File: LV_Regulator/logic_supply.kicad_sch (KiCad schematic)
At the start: 19 parts, among them IC2 MIC29152WU, IC3 MIC29152WU

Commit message: Added Footprints & Links for Component Purchase
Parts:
- C10, C7: footprint (none) -> Capacitor_SMD:C_1206_3216Metric_Pad1.33x1.80mm_HandSolder; Purchase Place (none) -> https://eu.mouser.com/ProductDetail/KYOCERA-AVX/12066G106ZA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
- C11, C8: footprint (none) -> Capacitor_SMD:C_1206_3216Metric_Pad1.33x1.80mm_HandSolder; Purchase Place (none) -> https://eu.mouser.com/ProductDetail/Murata-Electronics/GGM3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
- C9: footprint (none) -> Capacitor_SMD:C_1206_3216Metric_Pad1.33x1.80mm_HandSolder; Purchase Place (none) -> https://eu.mouser.com/ProductDetail/TAIYO-YUDEN/MLASJ319LB5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
- D2, D3, D4, D5: footprint (none) -> SS14:CR_SMA_403AE_OSI; Purchase Place (none) -> https://www.digikey.com/en/products/detail/onsemi/ss14/9654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
- F2, F3: footprint (none) -> Fuse:Fuse_1206_3216Metric_Pad1.42x1.75mm_HandSolder; Purchase Place (none) -> https://eu.mouser.com/ProductDetail/Bourns/SF-1206S100-2?qs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
- IC2, IC3: footprint MIC29152WU -> MIC29152WU:MIC29152WU
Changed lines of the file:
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@@
 			)
 		)
-		(property "Footprint" "MIC29152WU"
+		(property "Footprint" "MIC29152WU:MIC29152WU"
 			(at 109.22 134.29 0)
 			(effects
@@
 			)
 		)
-		(property "Footprint" ""
+		(property "Footprint" "SS14:CR_SMA_403AE_OSI"
 			(at 50.8 101.6 0)
 			(effects
@@
 		)
 		(property "Sim.Pins" "1=K 2=A"
+			(at 50.8 101.6 0)
+			(effects
+				(font
+					(size 1.27 1.27)
+				)
+				(hide yes)
+			)
+		)
+		(property "Purchase Place" "https://www.digikey.com/en/products/detail/onsemi/ss14/965474"
 			(at 50.8 101.6 0)
 			(effects
@@
 			)
 		)
-		(property "Footprint" ""
+		(property "Footprint" "Capacitor_SMD:C_1206_3216Metric_Pad1.33x1.80mm_HandSolder"
 			(at 82.2452 95.25 0)
 			(effects
@@
 		)
 		(property "Description" "Unpolarized capacitor"
+			(at 81.28 91.44 0)
+			(effects
+				(font
+					(size 1.27 1.27)
+				)
+				(hide yes)
+			)
+		)
+		(property "Purchase Place" "https://eu.mouser.com/ProductDetail/KYOCERA-AVX/12066G106ZAT4A?qs=f21FSZc47Pg9KHN6RDKhaQ%3D%3D"
 			(at 81.28 91.44 0)
 			(effects
@@
 			)
 		)
-		(property "Footprint" ""
+		(property "Footprint" "Fuse:Fuse_1206_3216Metric_Pad1.42x1.75mm_HandSolder"
 			(at 60.96 103.378 90)
 			(effects
@@
 		(property "Description" "Fuse"
 			(at 60.96 101.6 0)
+			(effects
+				(font
+					(size 1.27 1.27)
+				)
+				(hide yes)
+			)
+		)
+		(property "Purchase Place" "https://eu.mouser.com/ProductDetail/Bourns/SF-1206S100-2?qs=GIQXYiEeHGDIjBsMHQBJ8g%3D%3D"
+			(at 60.96 101.6 90)
 			(effects
 				(font
@@
 			)
 		)
-		(property "Footprint" ""
+		(property "Footprint" "Capacitor_SMD:C_1206_3216Metric_Pad1.33x1.80mm_HandSolder"
 			(at 42.8752 46.99 0)
 			(effects
@@
 		)
 		(property "Description" "Unpolarized capacitor"
+			(at 41.91 50.8 0)
+			(effects
+				(font
+					(size 1.27 1.27)
+				)
+				(hide yes)
+			)
+		)
+		(property "Purchase Place" "https://eu.mouser.com/ProductDetail/TAIYO-YUDEN/MLASJ319LB5476MTNA01?qs=tlsG%2FOw5FFj12GZbAd1Q9Q%3D%3D"
 			(at 41.91 50.8 0)
 			(effects
@@
 			)
 		)
-		(property "Footprint" "MIC29152WU"
+		(property "Footprint" "MIC29152WU:MIC29152WU"
 			(at 111.76 188.9 0)
 			(effects
@@
 			)
 		)
-		(property "Footprint" ""
+		(property "Footprint" "SS14:CR_SMA_403AE_OSI"
 			(at 50.8 46.99 0)
 			(effects
@@
 		)
 		(property "Sim.Pins" "1=K 2=A"
+			(at 50.8 46.99 0)
+			(effects
+				(font
+					(size 1.27 1.27)
+				)
+				(hide yes)
+			)
+		)
+		(property "Purchase Place" "https://www.digikey.com/en/products/detail/onsemi/ss14/965474"
 			(at 50.8 46.99 0)
 			(effects
@@
 			)
 		)
-		(property "Footprint" ""
+		(property "Footprint" "Capacitor_SMD:C_1206_3216Metric_Pad1.33x1.80mm_HandSolder"
 			(at 70.8152 101.6 0)
 			(effects
@@
 		)
 		(property "Description" "Unpolarized capacitor"
+			(at 69.85 105.41 0)
+			(effects
+				(font
+					(size 1.27 1.27)
+				)
+				(hide yes)
+			)
+		)
+		(property "Purchase Place" "https://eu.mouser.com/ProductDetail/Murata-Electronics/GGM31CD70J226KE02L?qs=efUn273yAheMi1mARkgjog%3D%3D"
 			(at 69.85 105.41 0)
 			(effects
@@
 			)
 		)
-		(property "Footprint" ""
+		(property "Footprint" "Capacitor_SMD:C_1206_3216Metric_Pad1.33x1.80mm_HandSolder"
 			(at 70.8152 46.99 0)
 			(effects
@@
 			)
 		)
+		(property "Purchase Place" "https://eu.mouser.com/ProductDetail/Murata-Electronics/GGM31CD70J226KE02L?qs=efUn273yAheMi1mARkgjog%3D%3D"
+			(at 69.85 50.8 0)
+			(effects
+				(font
+					(size 1.27 1.27)
+				)
+				(hide yes)
+			)
+		)
 		(pin "1"
 		)
@@
 			)
 		)
-		(property "Footprint" ""
+		(property "Footprint" "Capacitor_SMD:C_1206_3216Metric_Pad1.33x1.80mm_HandSolder"
 			(at 79.7052 40.64 0)
 			(effects
@@
 		)
 		(property "Description" "Unpolarized capacitor"
+			(at 78.74 36.83 0)
+			(effects
+				(font
+					(size 1.27 1.27)
+				)
+				(hide yes)
+			)
+		)
+		(property "Purchase Place" "https://eu.mouser.com/ProductDetail/KYOCERA-AVX/12066G106ZAT4A?qs=f21FSZc47Pg9KHN6RDKhaQ%3D%3D"
 			(at 78.74 36.83 0)
 			(effects
@@
 			)
 		)
-		(property "Footprint" ""
+		(property "Footprint" "SS14:CR_SMA_403AE_OSI"
 			(at 44.45 92.71 0)
 			(effects
@@
 		(property "Sim.Pins" "1=K 2=A"
 			(at 44.45 92.71 0)
+			(effects
+				(font
+					(size 1.27 1.27)
+				)
+				(hide yes)
+			)
+		)
+		(property "Purchase Place" "https://www.digikey.com/en/products/detail/onsemi/ss14/965474"
+			(at 44.45 92.71 90)
 			(effects
 				(font
@@
 			)
 		)
-		(property "Footprint" ""
+		(property "Footprint" "Fuse:Fuse_1206_3216Metric_Pad1.42x1.75mm_HandSolder"
 			(at 62.23 48.768 90)
 			(effects
@@
 		(property "Description" "Fuse"
 			(at 62.23 46.99 0)
+			(effects
+				(font
+					(size 1.27 1.27)
+				)
+				(hide yes)
+			)
+		)
+		(property "Purchase Place" "https://eu.mouser.com/ProductDetail/Bourns/SF-1206S100-2?qs=GIQXYiEeHGDIjBsMHQBJ8g%3D%3D"
+			(at 62.23 46.99 90)
 			(effects
 				(font
@@
 			)
 		)
-		(property "Footprint" ""
+		(property "Footprint" "SS14:CR_SMA_403AE_OSI"
 			(at 44.45 39.37 0)
 			(effects
@@
 			(effects
 				(font
+					(size 1.27 1.27)
+				)
+				(hide yes)
+			)
+		)
+		(property "Purchase Place" "https://www.digikey.com/en/products/detail/onsemi/ss14/965474"
+			(at 44.45 39.37 90)
+			(effects
+				(font

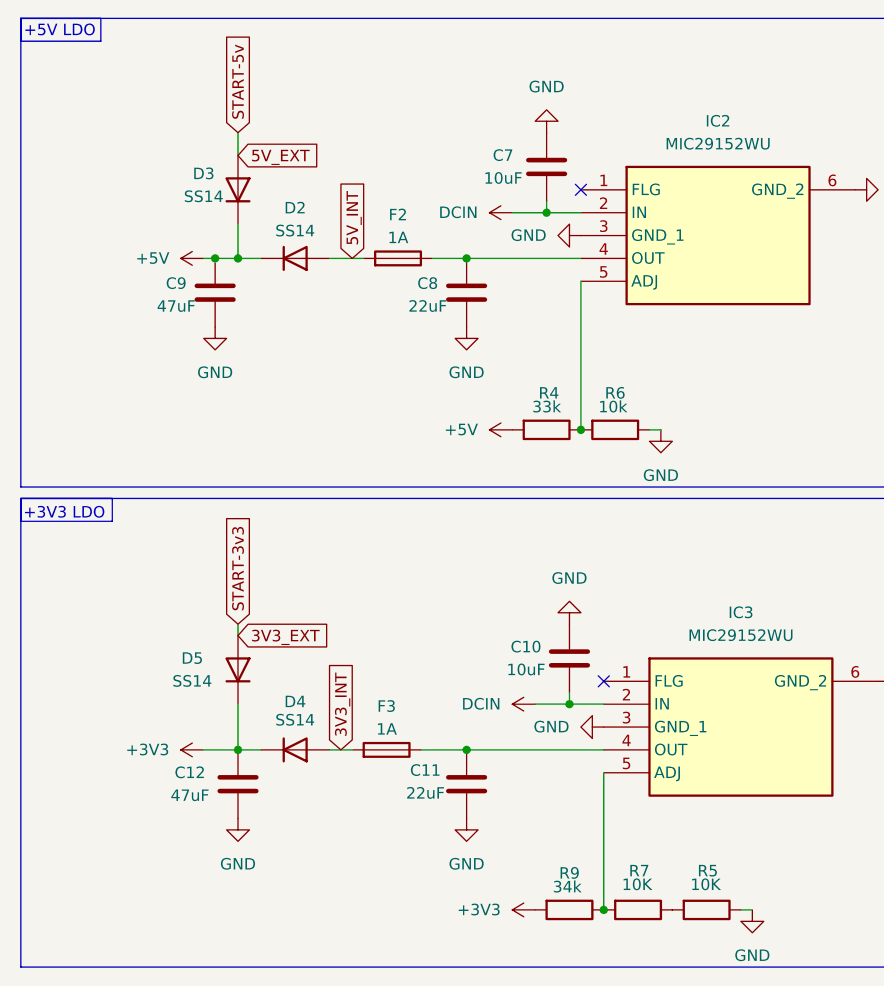
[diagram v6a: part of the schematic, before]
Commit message: Halfway Push of adding 3D models to PCB layout components
Pushing with components left to add to finish on main PC
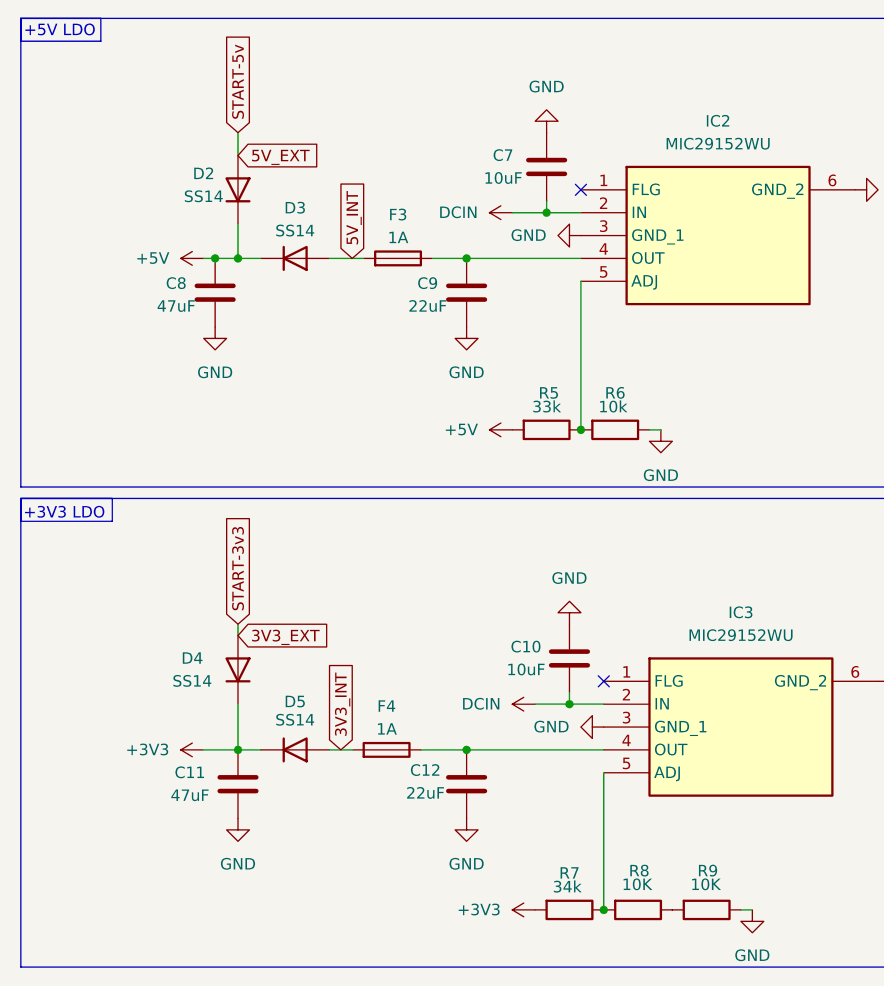
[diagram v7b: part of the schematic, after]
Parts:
- C11: renamed from C12; footprint (none) -> Capacitor_SMD:C_1206_3216Metric_Pad1.33x1.80mm_HandSolder; Purchase Place (none) -> https://eu.mouser.com/ProductDetail/TAIYO-YUDEN/MLASJ319LB5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
- renumbered C11 to C12, C9 to C8, C8 to C9, D3 to D2, D2 to D3, D5 to D4, D4 to D5, F2 to F3, F3 to F4, R4 to R5, R9 to R7, R7 to R8, R5 to R9

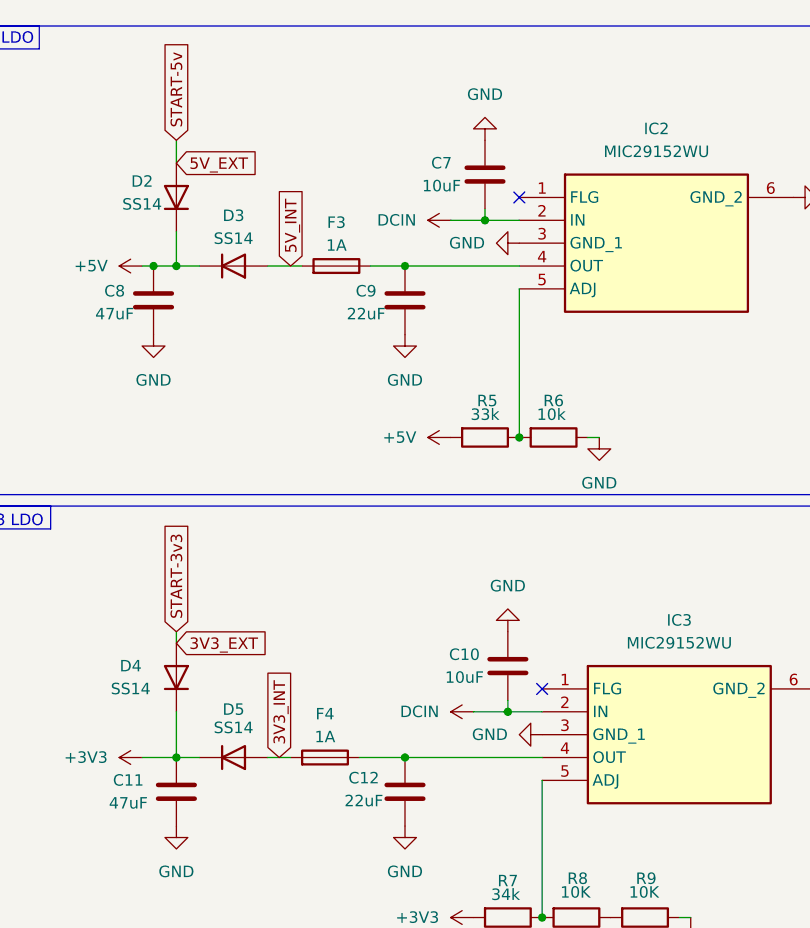
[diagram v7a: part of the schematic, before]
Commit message: Multiple Fixes in Schematic & Routing
Fixed multiple issues in schematic, like adding jumpers to isolate ACUV/ACOV between the choices. Moved the fuses on the Logic_Supply as per instruction of professor from Chair of Electronics, FoTS, UoNS. Started and made good progress on Power Electronics (Regulator Side) of the PCB.
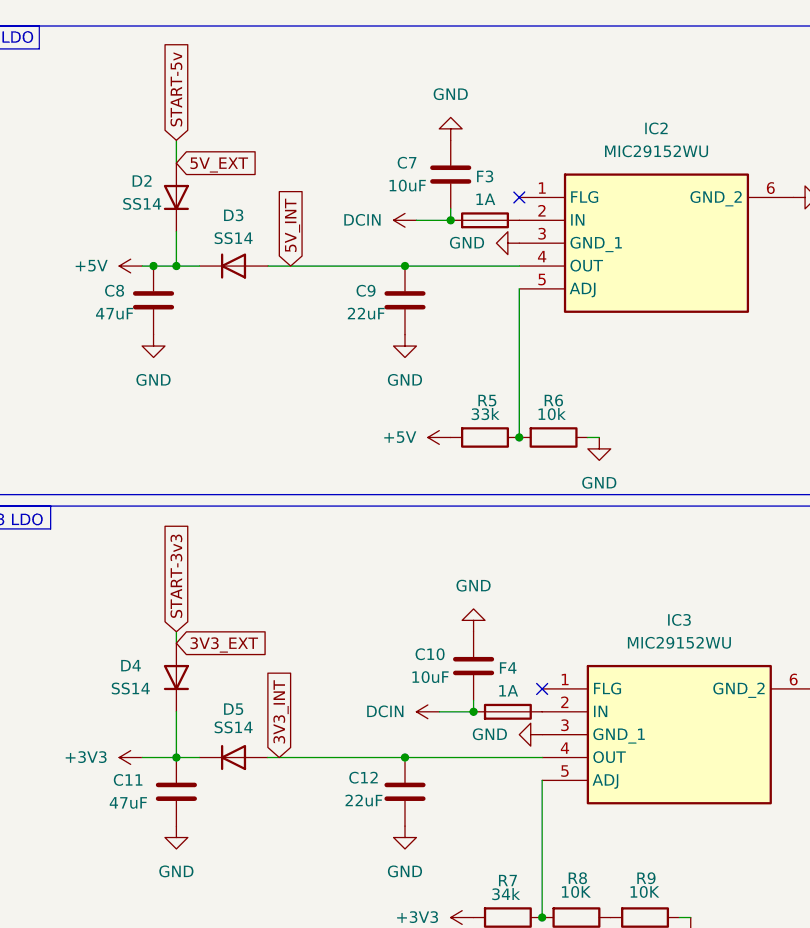
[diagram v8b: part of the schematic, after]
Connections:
- net 3V3_INT: now also C12.2, IC3.4 (OUT); no longer F4.2
- net 5V_INT: now also C9.2, IC2.4 (OUT); no longer F3.2
- net DCIN: now also F3.2, F4.2; no longer IC2.2 (IN), IC3.2 (IN)
- new net: F3.1, IC2.2 (IN)
- new net: F4.1, IC3.2 (IN)
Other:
- moved on the sheet: C10, C7, F3, F4
